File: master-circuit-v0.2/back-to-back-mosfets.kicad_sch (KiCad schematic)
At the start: 6 parts

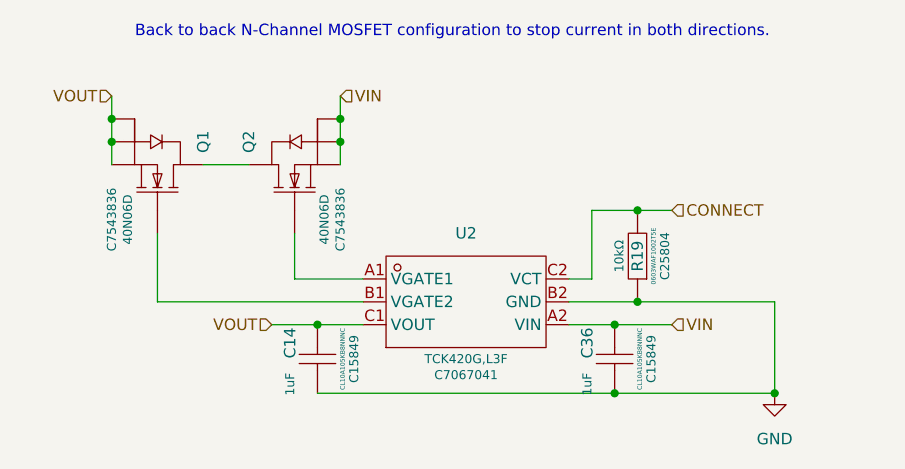
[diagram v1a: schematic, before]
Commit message: Connect one of the USB outputs, outline part placement.
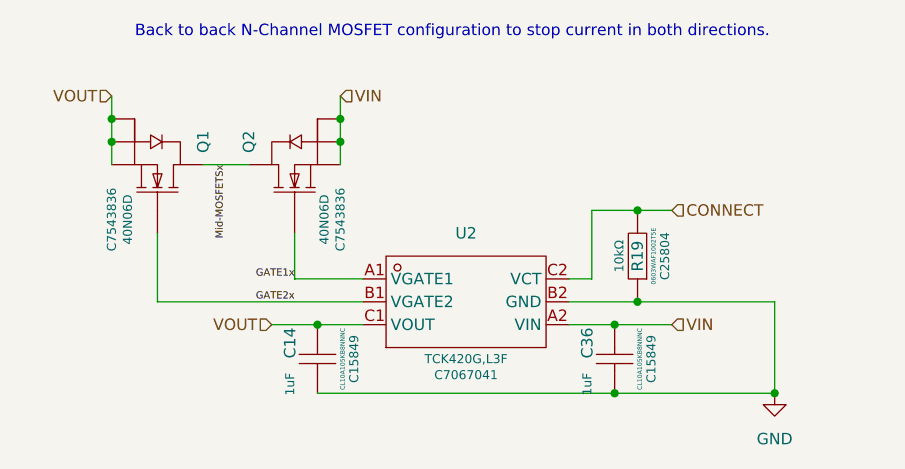
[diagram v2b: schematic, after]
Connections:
- net GATE1x: now reaches Q2.4 (G), U2.A1 (VGATE1)
- net GATE2x: now reaches Q1.4 (G), U2.B1 (VGATE2)
- net Mid-MOSFETSx: now reaches Q1.5 (D), Q2.5 (D)
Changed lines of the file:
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@@
+		)
+	)
+	(label "GATE2x"
+		(at 101.6 92.71 180)
+		(effects
+			(font
+				(size 0.8 0.8)
+			)
+			(justify right bottom)
+		)
+	)
+	(label "Mid-MOSFETSx"
+		(at 93.98 77.47 270)
+		(effects
+			(font
+				(size 0.8 0.8)
+			)
+			(justify right bottom)
+		)
+	)
+	(label "GATE1x"
+		(at 101.6 90.17 180)
+		(effects
+			(font
+				(size 0.8 0.8)
+			)
+			(justify right bottom)
 		)
 	)
